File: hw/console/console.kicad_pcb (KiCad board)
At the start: 2 copper layers, 156 x 74 mm, 161 parts, among them J1 Batt, J301 USB-C 16P, J401 DM3AT-SF-PEJM5, J501 SPK 8R, J601 FFC-40 0.5mm, J901 UART, Q601 AO3400A, SW1 Движок, SW101 UP, SW102 DOWN, SW103 LEFT, SW104 RIGHT, SW105 SELECT, SW106 START, SW107 A, SW108 B, SW109 C, SW110 D, U1 F133-A, U2 SY8089AAAC, U3 SY8089AAAC, U4 SY8089AAAC, U401 W25Q32JVSSIQ, U5 TP4056, U501 PAM8301, Y1 24 МГц, Y2 32.768 кГц

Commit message: hw: microSD и UART переставлены по распиновке, а не по удобству торца
`fanout.py` — новый разбор — считает для каждого вывода F133, с какой стороны
корпуса он выходит и куда зовёт его цепь. Ответ: **52 сигнала из 90 идут
вокруг корпуса**, и сорок из них просятся налево, выходя вверх и вправо.

Причина оказалась записана в нашем же документе, в двух местах и по-разному.
§5.1 говорит: банк хранения `PF`/`PC` выходит вправо, отладка `PE` — вверх.
§5 ставит microSD в левый верхний угол, а UART в левый нижний. Семь линий
карты и шесть линий отладки шли через всю плату вокруг чипа.

Переставлено по распиновке: `J401` на верхний торец справа (x = 132), `J901`
туда же левее (x = 100) и положена вдоль реза — стоймя гребёнка уходит на
11.2 мм вглубь при полосе вне панели в 9.7, а высота у неё 8.5 мм, она упёрлась
бы в стекло. Зоны блоков 4 и 9 переехали под свои разъёмы.

Стало 45 против 52. Остаток — крестовина: её линии выходят у чипа вправо, а
сами кнопки на левом краю по эргономике, и это не переставить.

Ещё: `pcb07_dsn.py` теперь переписывает посадку деталей в задании по нынешней
плате. Экспорт `.dsn` делается руками из KiCad, и без этого каждая правка
размещения требовала бы снова лезть в KiCad. Проверено: переписанная секция
совпадает с кикадовской побайтово.

Число проходов freerouting берёт из `FREEROUTING__ROUTER__STOP_PASS_NO` —
именно из него, а не из `MAX_PASSES`, как я решил по единственному удачному
прогону, где задал оба сразу.

Co-Authored-By: Claude Opus 5 <noreply@anthropic.com>
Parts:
- moved J401 106.0 mm to (182.0, 48.9)
- moved J901 101.7 mm to (150.0, 41.8), turned to 90 degrees
- moved R402 34.3 mm to (196.0, 59.5)
- moved R406 29.7 mm to (191.4, 62.2)
- moved R407 29.7 mm to (195.9, 62.2)
- moved R411 25.3 mm to (191.4, 64.9)
- moved R410 25.3 mm to (186.9, 64.9)
- moved R901 19.1 mm to (134.4, 55.8)
- moved D901 19.1 mm to (129.9, 55.8)
- moved R401 17.3 mm to (191.5, 59.5)
- moved C401 17.3 mm to (177.9, 59.5)
- moved C402 17.3 mm to (182.5, 59.5)
- moved C403 17.3 mm to (187.0, 59.5)
- moved R405 13.2 mm to (186.9, 62.2)
- moved R403 13.2 mm to (177.9, 62.2)
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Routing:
- net GND: track 569.2 -> 0.00 mm, vias 86 -> 108
- net +3V3: track 262.1 -> 0.00 mm, vias 6 -> 0
- net VSYS: track 123.2 -> 0.00 mm, vias 3 -> 0
- net SDC0-D1: track 103.7 -> 0.00 mm, vias 2 -> 0
- net SD-CLK: track 103.0 -> 0.00 mm, vias 2 -> 0
- net SPI0-MOSI: track 97.5 -> 0.00 mm, vias 2 -> 0
- net SDC0-CMD: track 91.9 -> 0.00 mm, vias 2 -> 0
- net SDC0-DET: track 91.0 -> 0.00 mm, vias 3 -> 0
- net EN_1V8: track 78.0 -> 0.00 mm, vias 2 -> 0
- net Net-(C4-Pad1): track 52.8 -> 0.00 mm
- net HPOUTL: track 50.9 -> 0.00 mm, vias 2 -> 0
- net VBUS: track 50.7 -> 0.00 mm
- net EN_3V3: track 49.3 -> 0.00 mm
- net Net-(C10-Pad1): track 47.5 -> 0.00 mm
- net Net-(C5-Pad1): track 44.8 -> 0.00 mm
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
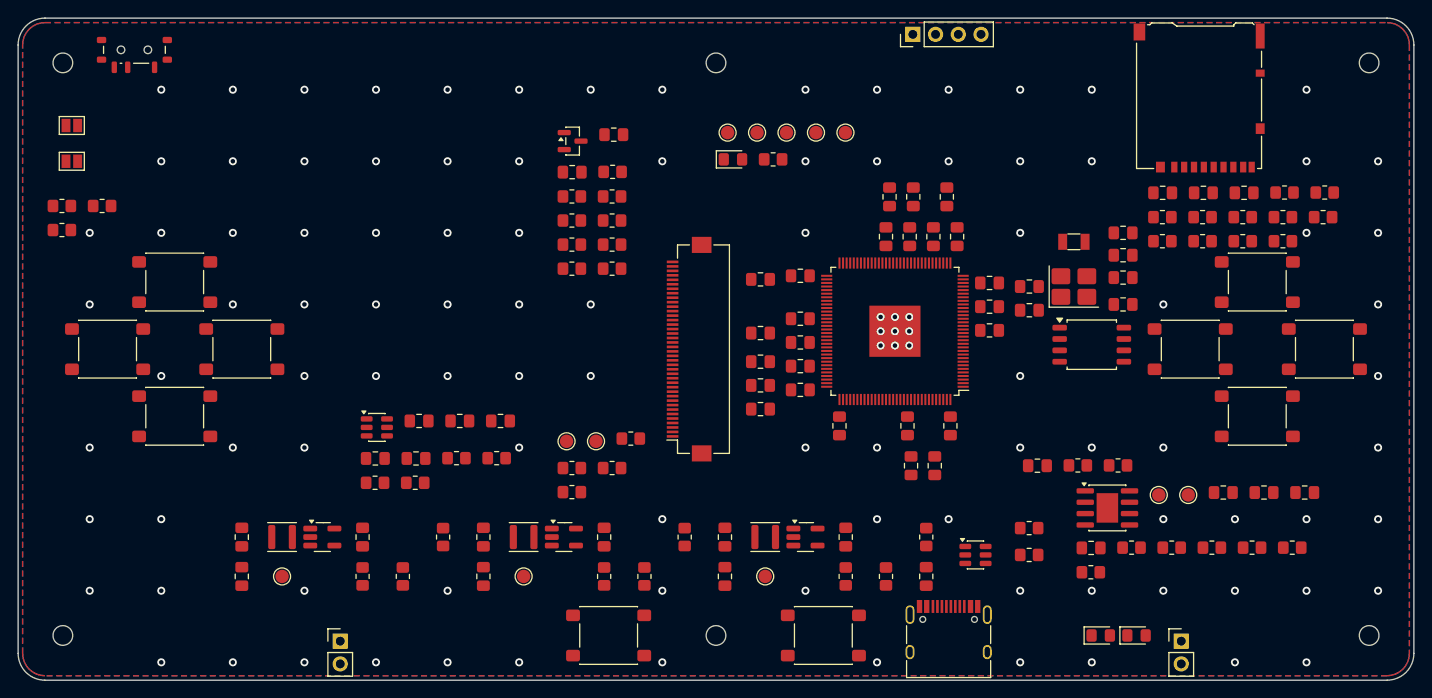
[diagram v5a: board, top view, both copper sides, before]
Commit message: hw: вывод из-под F133 делаем сами — трассировщик его не делает вовсе
Freerouting не развёл ни одной связи чипа ни в одном прогоне. Не «плохо
развёл» — **ни одной**: посчитал по ответу, из 128 площадок медь не пришла ни
к одной. В логе на каждый проход десятки `NullPointerException` из
`MazeSearchAlgo.expand_to_target_doors` — он роняет свой поиск пути всякий
раз, когда целью оказывается площадка с шагом 0.4 мм.

Это объясняет всё, во что мы упирались: сотня неразведённых связей держалась
одинаково при любых зазорах, переходных и числе проходов, потому что упор был
не в тесноту.

`pcb07_fanout.py` выводит сигналы сам: от каждой площадки короткий луч наружу,
концы через один на двух радиусах — иначе они стоят тем же частоколом 0.4 мм и
подойти к концу сбоку так же нельзя, как к самой площадке. Длину каждый луч
подбирает себе, укорачиваясь до ближайшей чужой меди: конденсаторы развязки
стоят вплотную к выводам, так и задумано. 65 лучей встали, 25 выводам места
не хватило — у них конденсатор ближе самого короткого луча.

После этого исключения прекратились, а разрывов с участием U1 стало 35 вместо
112.

Задание отдаёт лучи неприкосновенной медью (секция `wiring` пересобирается по
плате, как и посадка), а приём их не трогает: freerouting неприкосновенную медь
обратно не возвращает, и снеси их приёмник — половина работы пропала бы молча.

Убрано послабление зазора до 185 мкм: в задании его иначе как на всю плату не
задать, и трассировщик поджимал 0.185 у чужих деталей — 32 нарушения вдали от
чипа. Под самим чипом оно теперь не нужно, там наши лучи, а исключение для них
в `console.kicad_dru` записано адресно.

Переходная разводки — 0.7/0.4 вместо 0.9/0.5, тоже по измерению: с крупной он
поставил одну штуку на всю плату и остался в одном слое, потому что 0.9 плюс
зазор с двух сторон это круг 1.3 мм, которому в тесноте негде встать.

Co-Authored-By: Claude Opus 5 <noreply@anthropic.com>
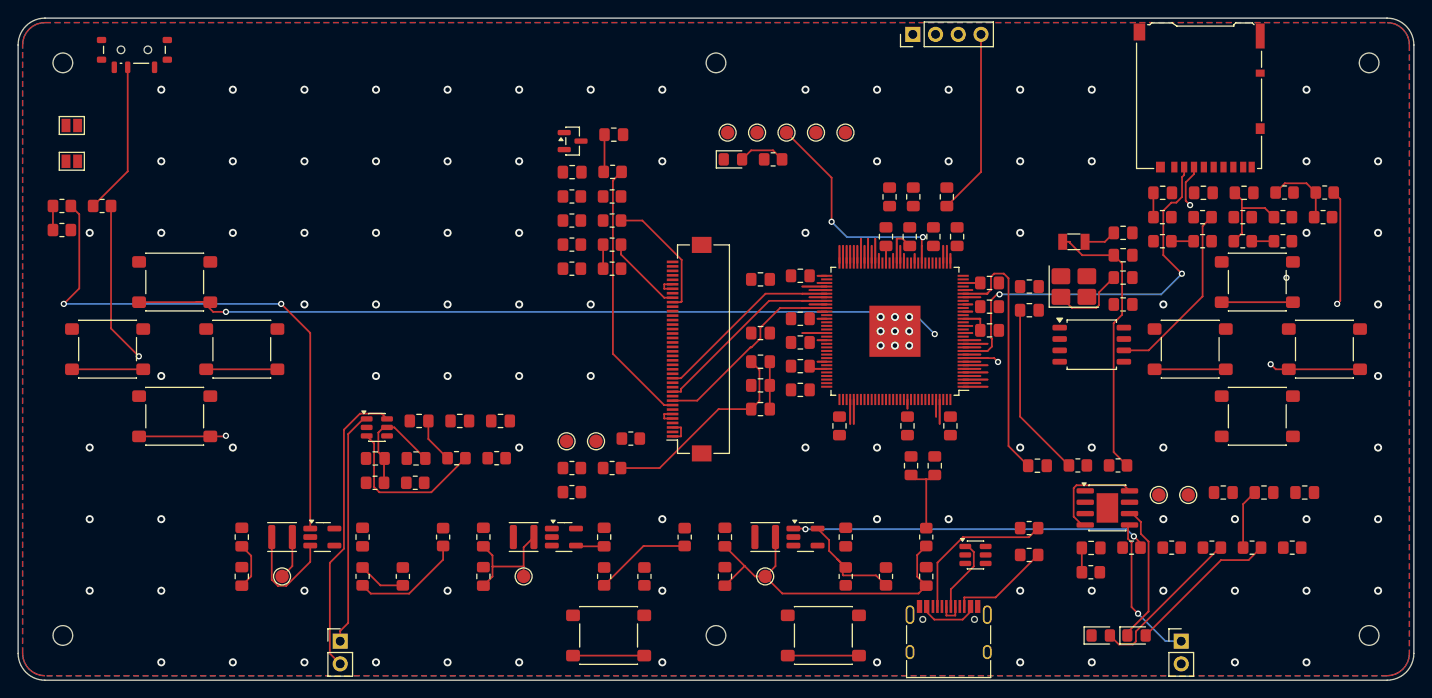
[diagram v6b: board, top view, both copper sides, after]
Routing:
- net KEY-UP: track 0.00 -> 97.4 mm, vias 0 -> 2
- net EN_3V3: track 0.00 -> 62.8 mm, vias 0 -> 2
- net +3V3: track 0.00 -> 57.0 mm
- net SDC0-D3: track 0.00 -> 48.0 mm, vias 0 -> 2
- net EN_0V9: track 0.00 -> 40.0 mm, vias 0 -> 2
- net +1V8: track 0.00 -> 40.0 mm
- net Net-(C10-Pad1): track 0.00 -> 38.3 mm
- net Net-(J501-Pin_2): track 0.00 -> 33.1 mm
- net RESET: track 0.00 -> 31.7 mm
- net X32KIN: track 0.00 -> 31.3 mm
- net LCD-LEDA: track 0.00 -> 29.8 mm
- net TDO: track 0.00 -> 27.8 mm, vias 0 -> 2
- net Net-(J501-Pin_1): track 0.00 -> 26.3 mm
- net AVCC: track 0.00 -> 25.4 mm
- net VBUS: track 0.00 -> 25.0 mm
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
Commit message: hw: луч умеет уходить наискось, и меряется по всем площадкам, включая свои
Двум десяткам выводов прямой луч не влезал — конденсатор развязки стоит
ближе. Добавлено отклонение конца вбок, и с ним же вылезли две своих ошибки:

* проверка смотрела только чужие площадки, а площадки самого F133 были
  исключены целиком — луч наискось садился прямо на соседний вывод чипа, и
  проверка молчала. Теперь в списке все, но с разной меркой: чужим общий зазор
  платы, выводам чипа послабление 0.15 из `console.kicad_dru`;
* лучи не знали друг о друге и пересекались. Мерка между осями — 0.4 мм, ровно
  столько между соседними по построению, поэтому берём волосок меньше, иначе
  каждый луч считает соседа помехой и веер не строится вовсе.

Скрипт теперь начинает с чистой меди: он первый шаг разводки, а вся разводка
всё равно кладётся заново из `.ses`.

Итог: 65 лучей, ноль нарушений DRC.

Co-Authored-By: Claude Opus 5 <noreply@anthropic.com>
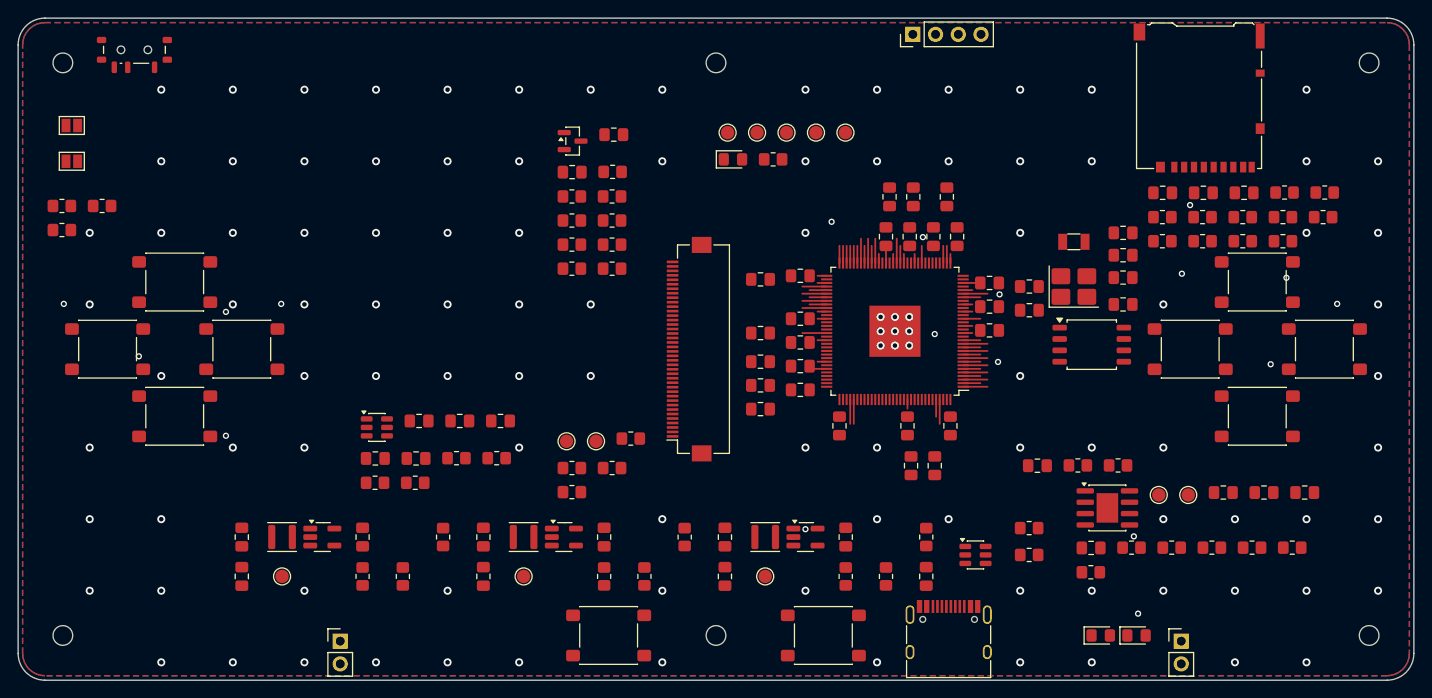
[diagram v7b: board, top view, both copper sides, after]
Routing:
- net KEY-UP: track 97.4 -> 2.72 mm
- net EN_3V3: track 62.8 -> 0.00 mm
- net +3V3: track 57.0 -> 2.95 mm
- net SDC0-D3: track 48.0 -> 2.72 mm
- net EN_0V9: track 40.0 -> 0.00 mm
- net Net-(C10-Pad1): track 38.3 -> 0.00 mm
- net Net-(J501-Pin_2): track 33.1 -> 0.00 mm
- net +1V8: track 40.0 -> 8.63 mm
- net X32KIN: track 31.3 -> 0.00 mm
- net LCD-LEDA: track 29.8 -> 0.00 mm
- net RESET: track 31.7 -> 2.72 mm
- net Net-(J501-Pin_1): track 26.3 -> 0.00 mm
- net TDO: track 27.8 -> 1.92 mm, vias 2 -> 1
- net VBUS: track 25.0 -> 0.00 mm
- net Net-(C5-Pad1): track 24.4 -> 0.00 mm
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
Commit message: hw: питание разводим сами — и свой трассировщик наконец кладёт медь
Питание оказалось второй половиной того, что freerouting не вытягивает: у
`+3V3` тридцать восемь площадок, у `+1V8` шестнадцать, у `+0V9` двенадцать.
Это не связь, а куст, и форма ответа известна заранее — дерево.

Сперва написал `pcb07_power.py`: дерево по Приму, связи прямой, углом и косым
коленом, каждая проверяется на просвет. Из восьмидесяти связей проходит
тринадцать — в кольце развязки прямой не пройти нигде, там всюду чужие
выводы. Оставлен как есть: он честно показывает, что задача не геометрическая,
а трассировочная.

Её и решает `pcb10_route.py`, свой волновой, — ему теперь можно дать список
цепей, а всю прочую медь он считает неприкосновенной помехой. 96 связей
питания, 157 отрезков, ноль нарушений DRC, неподключённых на плате стало 227
вместо 283.

И там же нашлись две своих ошибки, из-за которых он раньше «работал»:

* `lay_rec` записывал путь без номера цепи, а `codeobj` не существовал вовсе —
  укладка на плату молча не делала ничего;
* соединённое он не отличал от «меди вообще», а в меди у цепи лежат все её
  площадки сразу. Цель оказывалась достигнутой в ноль шагов: путь пустой,
  счётчик растёт, дорожек нет. Разводка «удавалась» на сто процентов и не
  давала ни одной дорожки — ровно то, что я принимал за слабость алгоритма.

Co-Authored-By: Claude Opus 5 <noreply@anthropic.com>
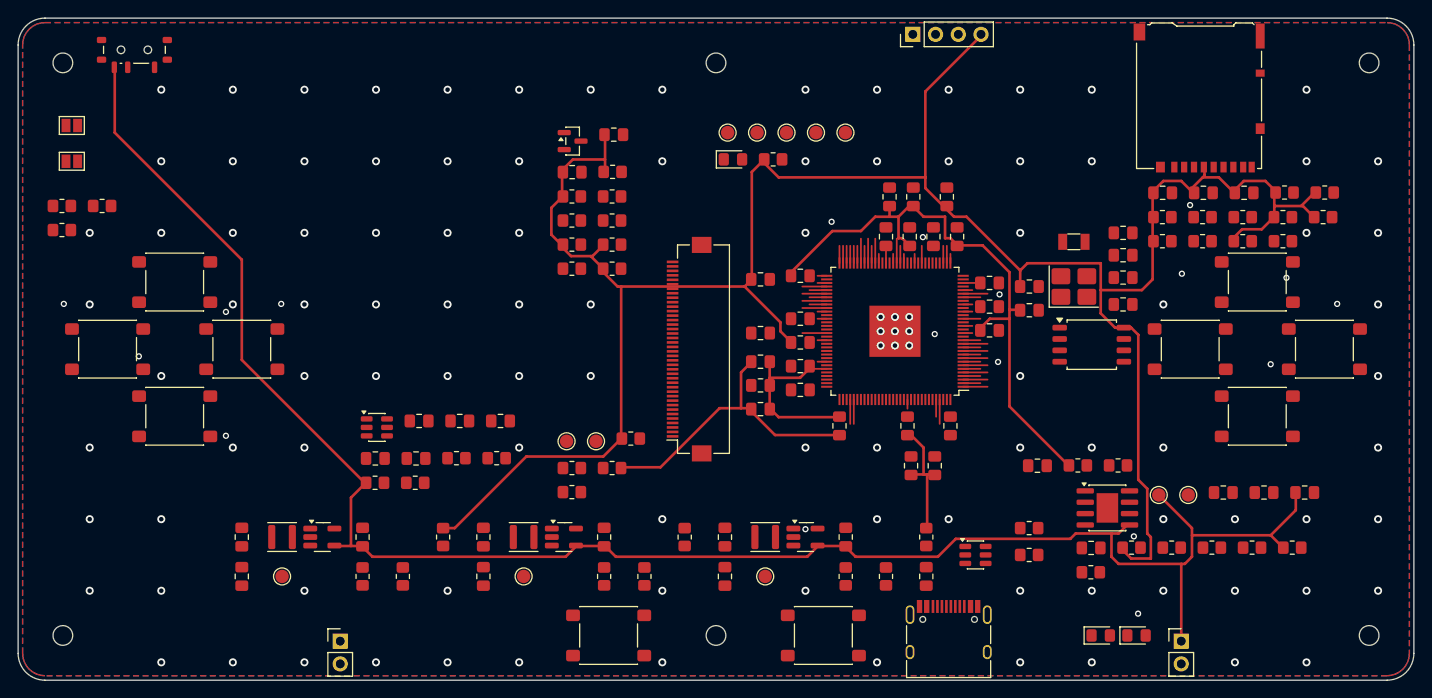
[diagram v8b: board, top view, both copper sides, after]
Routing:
- net +3V3: track 2.95 -> 266.9 mm
- net VSYS: track 0.00 -> 204.8 mm
- net +1V8: track 8.63 -> 75.6 mm
- net AVCC: track 1.03 -> 35.3 mm
- net AGND: track 1.93 -> 20.6 mm
- net +0V9: track 6.70 -> 20.7 mm
